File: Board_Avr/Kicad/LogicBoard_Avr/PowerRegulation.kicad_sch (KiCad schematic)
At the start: 8 parts, among them J10 PSU Connector, U3 LM1117-3.3, U4 LM1117-5.0

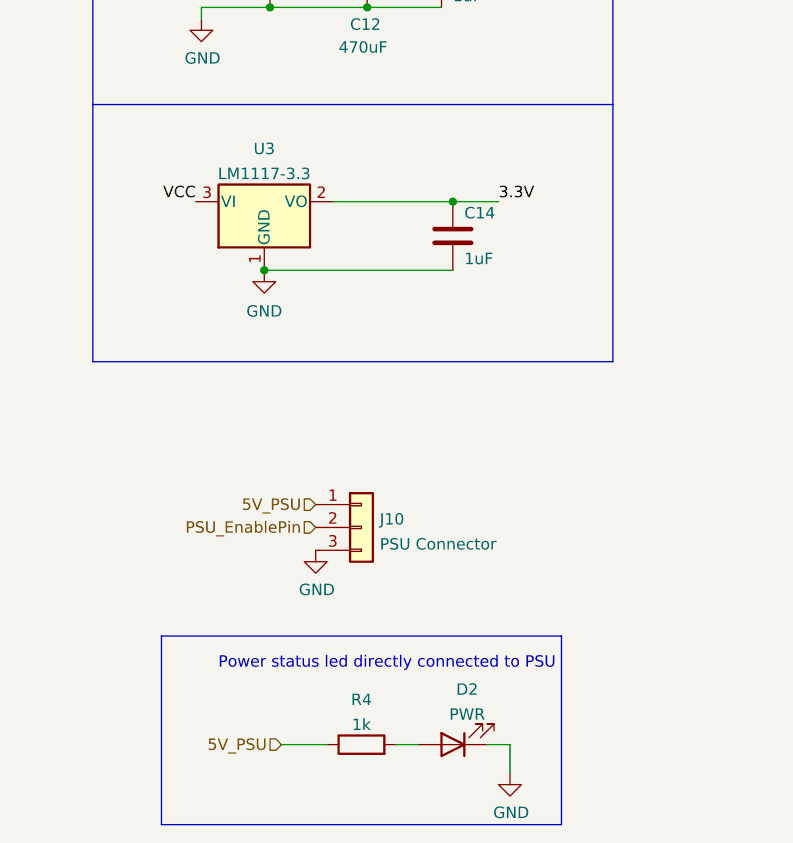
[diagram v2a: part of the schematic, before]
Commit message: Started routing all traces
Signed-off-by: bebenlebricolo <benoittarrade@hotmail.fr>
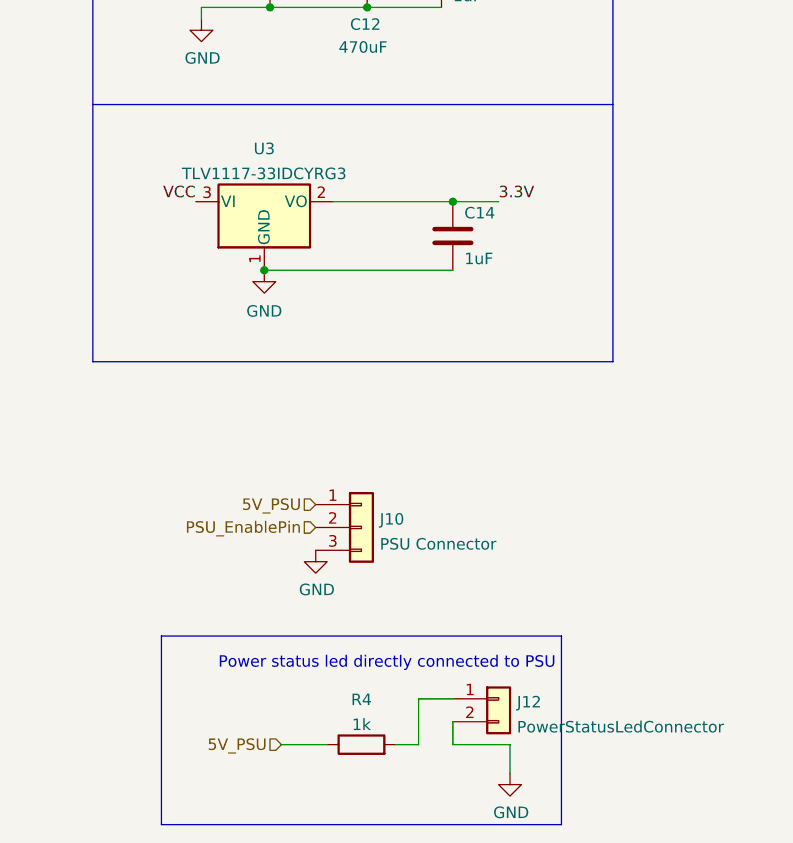
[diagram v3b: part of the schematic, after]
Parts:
- removed D2: PWR, symbol Device:LED
- added J12: PowerStatusLedConnector, Connector_PinHeader_2.54mm:PinHeader_1x02_P2.54mm_Vertical, symbol Connector_Generic:Conn_01x02
- C12: footprint (none) -> Capacitor_SMD:C_Elec_8x6.2
- C13, C14: footprint Capacitor_SMD:C_1206_3216Metric_Pad1.33x1.80mm_HandSolder -> Capacitor_SMD:C_1206_3216Metric
- J10: footprint (none) -> BTS-LogicBoard:559350310
- R4: footprint (none) -> Resistor_SMD:R_1206_3216Metric_Pad1.30x1.75mm_HandSolder
- U3: value LM1117-3.3 -> TLV1117-33IDCYRG3; footprint (none) -> Package_TO_SOT_SMD:SOT-223-3_TabPin2
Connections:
- net GND: now also J12.2 (Pin_2)
- net at R4.2: now also J12.1 (Pin_1)
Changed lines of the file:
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@@
+    (stroke (width 0) (type default) (color 0 0 0 0))
+  )
+  (wire (pts (xy 164.465 118.11) (xy 168.275 118.11))
     (stroke (width 0) (type default) (color 0 0 0 0))
   )
@@
     (stroke (width 0) (type default) (color 0 0 0 0))
   )
+  (wire (pts (xy 164.465 123.19) (xy 164.465 118.11))
+    (stroke (width 0) (type default) (color 0 0 0 0))
+  )
   (polyline (pts (xy 180.34 132.08) (xy 135.89 132.08))
     (stroke (width 0) (type default) (color 0 0 0 0))
@@
     (stroke (width 0) (type default) (color 0 0 0 0))
   )
+  (wire (pts (xy 168.275 120.65) (xy 168.275 123.19))
+    (stroke (width 0) (type default) (color 0 0 0 0))
+  )
   (wire (pts (xy 147.32 70.485) (xy 168.275 70.485))
     (stroke (width 0) (type default) (color 0 0 0 0))
@@
     (stroke (width 0) (type default) (color 0 0 0 0))
   )
-  (wire (pts (xy 172.085 123.19) (xy 174.625 123.19))
+  (wire (pts (xy 168.275 123.19) (xy 174.625 123.19))
     (stroke (width 0) (type default) (color 0 0 0 0))
   )
@@
     (in_bom yes) (on_board yes) (fields_autoplaced)
     (property "Reference" "U3" (id 0) (at 147.32 56.9935 0))
-    (property "Value" "LM1117-3.3" (id 1) (at 147.32 59.7686 0))
-    (property "Footprint" "" (id 2) (at 147.32 62.865 0)
+    (property "Value" "TLV1117-33IDCYRG3" (id 1) (at 147.32 59.7686 0))
+    (property "Footprint" "Package_TO_SOT_SMD:SOT-223-3_TabPin2" (id 2) (at 147.32 62.865 0)
       (effects (font (size 1.27 1.27)) hide)
     )
@@
       (effects (font (size 1.27 1.27)) (justify left))
     )
-    (property "Footprint" "Capacitor_SMD:C_1206_3216Metric_Pad1.33x1.80mm_HandSolder" (id 2) (at 167.9702 41.275 0)
+    (property "Footprint" "Capacitor_SMD:C_1206_3216Metric" (id 2) (at 167.9702 41.275 0)
       (effects (font (size 1.27 1.27)) hide)
     )
@@
       (effects (font (size 1.27 1.27)) (justify left))
     )
-    (property "Footprint" "Capacitor_SMD:C_1206_3216Metric_Pad1.33x1.80mm_HandSolder" (id 2) (at 169.2402 70.485 0)
+    (property "Footprint" "Capacitor_SMD:C_1206_3216Metric" (id 2) (at 169.2402 70.485 0)
       (effects (font (size 1.27 1.27)) hide)
     )
@@
       (effects (font (size 1.27 1.27)) (justify left))
     )
-    (property "Footprint" "" (id 2) (at 158.115 99.06 0)
+    (property "Footprint" "BTS-LogicBoard:559350310" (id 2) (at 158.115 99.06 0)
       (effects (font (size 1.27 1.27)) hide)
     )
@@
     (property "Reference" "R4" (id 0) (at 158.115 118.2075 90))
     (property "Value" "1k" (id 1) (at 158.115 120.9826 90))
-    (property "Footprint" "" (id 2) (at 158.115 124.968 90)
+    (property "Footprint" "Resistor_SMD:R_1206_3216Metric_Pad1.30x1.75mm_HandSolder" (id 2) (at 158.115 124.968 90)
       (effects (font (size 1.27 1.27)) hide)
     )
@@
     (pin "2")
   )
-  (symbol (lib_id "Device:LED") (at 168.275 123.19 180) (unit 1)
-    (in_bom yes) (on_board yes) (fields_autoplaced)
-    (property "Reference" "D2" (id 0) (at 169.8625 117.0645 0))
-    (property "Value" "PWR" (id 1) (at 169.8625 119.8396 0))
-    (property "Footprint" "" (id 2) (at 168.275 123.19 0)
-      (effects (font (size 1.27 1.27)) hide)
-    )
-    (property "Datasheet" "~" (id 3) (at 168.275 123.19 0)
+  (symbol (lib_id "Connector_Generic:Conn_01x02") (at 173.355 118.11 0) (unit 1)
+    (in_bom yes) (on_board yes) (fields_autoplaced)
+    (property "Reference" "J12" (id 0) (at 175.387 118.4715 0)
+      (effects (font (size 1.27 1.27)) (justify left))
+    )
+    (property "Value" "PowerStatusLedConnector" (id 1) (at 175.387 121.2466 0)
+      (effects (font (size 1.27 1.27)) (justify left))
+    )
+    (property "Footprint" "Connector_PinHeader_2.54mm:PinHeader_1x02_P2.54mm_Vertical" (id 2) (at 173.355 118.11 0)
+      (effects (font (size 1.27 1.27)) hide)
+    )
+    (property "Datasheet" "~" (id 3) (at 173.355 118.11 0)
       (effects (font (size 1.27 1.27)) hide)
     )
@@
       (effects (font (size 1.27 1.27)) (justify left))
     )
-    (property "Footprint" "" (id 2) (at 159.7152 41.275 0)
-      (effects (font (size 1.27 1.27)) hide)
-    )
+    (property "Footprint" "Capacitor_SMD:C_Elec_8x6.2" (id 2) (at 159.7152 41.275 0)
+      (effects (font (size 1.27 1.27)) hide)
+    )

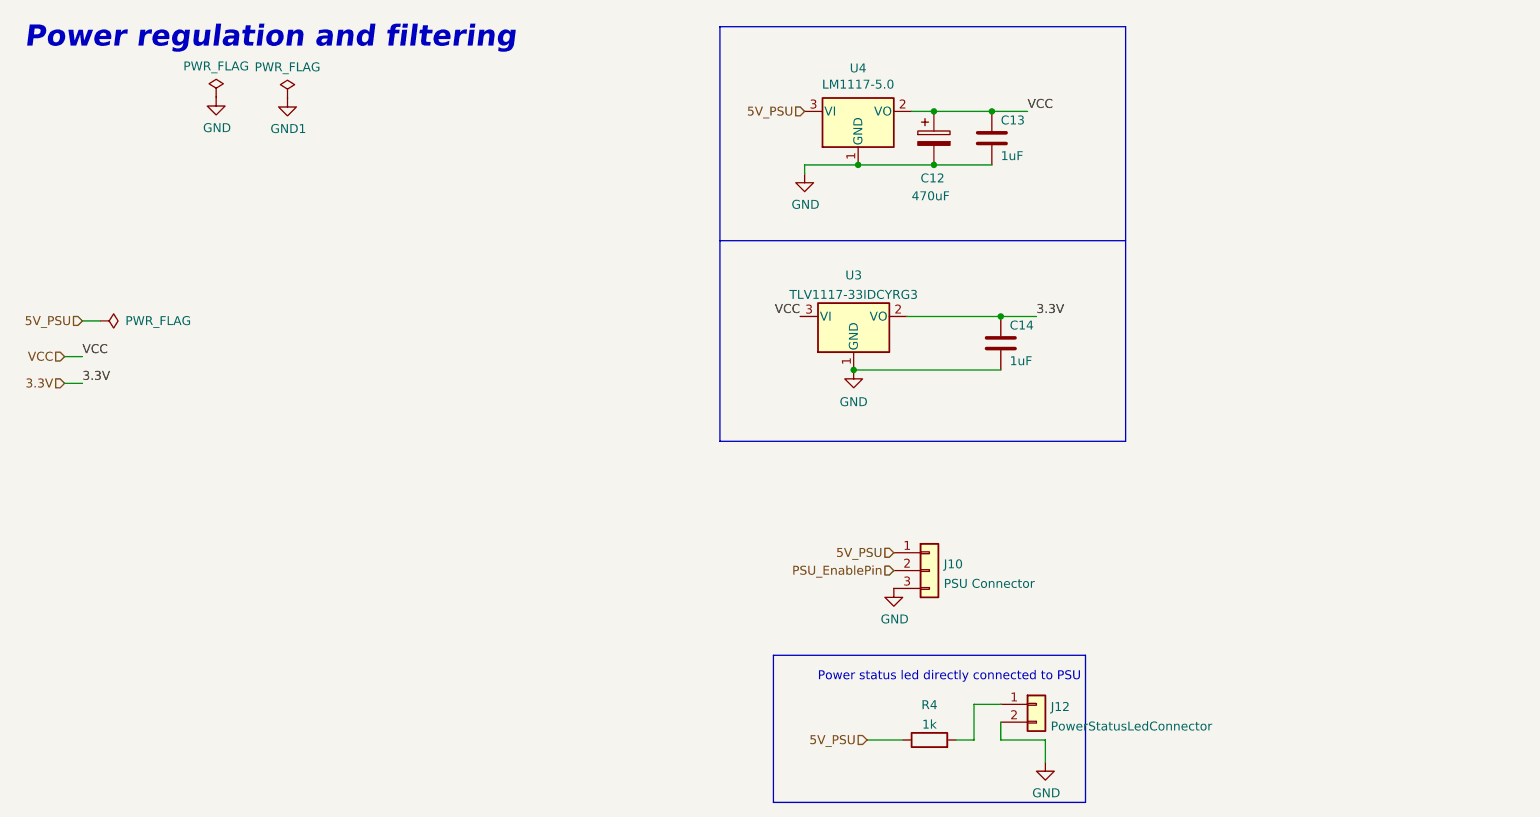
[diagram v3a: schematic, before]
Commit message: Tweaked top silkscreen to embed useful information
Signed-off-by: bebenlebricolo <benoittarrade@hotmail.fr>
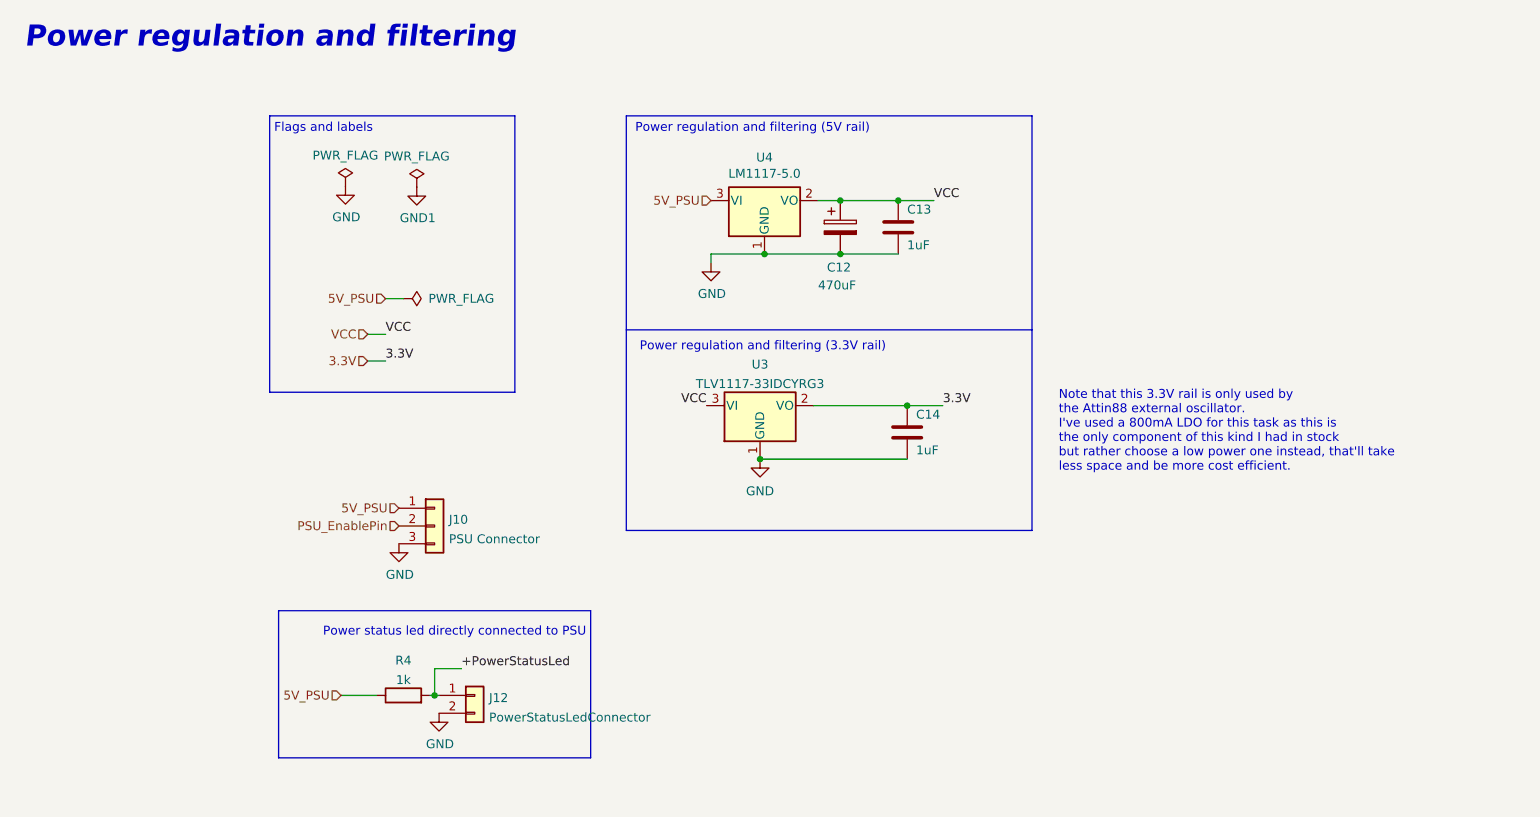
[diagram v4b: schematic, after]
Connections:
- net +PowerStatusLed: now reaches J12.1 (Pin_1), R4.2
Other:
- note added: "Flags and labels"
- note added: "Note that this 3.3V rail is only used by the Attin88 external oscillator. I've used a 800mA LDO for this task as this is the only component of this kind I had in stock but rather choose a low power one instead, that'll take less space and be more cost efficient."
- note added: "Power regulation and filtering (3.3V rail)"
- note added: "Power regulation and filtering (5V rail)"
- moved on the sheet: C12, C13, C14, J10, J12, R4, U3, U4

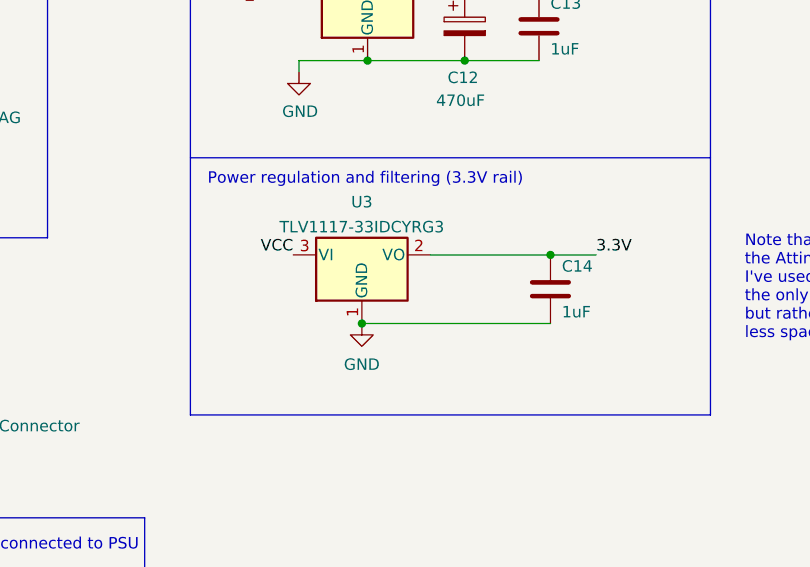
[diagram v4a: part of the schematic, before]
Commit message: Replaced TLV1117-3.3 by NCP630SN330 and polished a bit zoning
Signed-off-by: bebenlebricolo <benoittarrade@hotmail.fr>
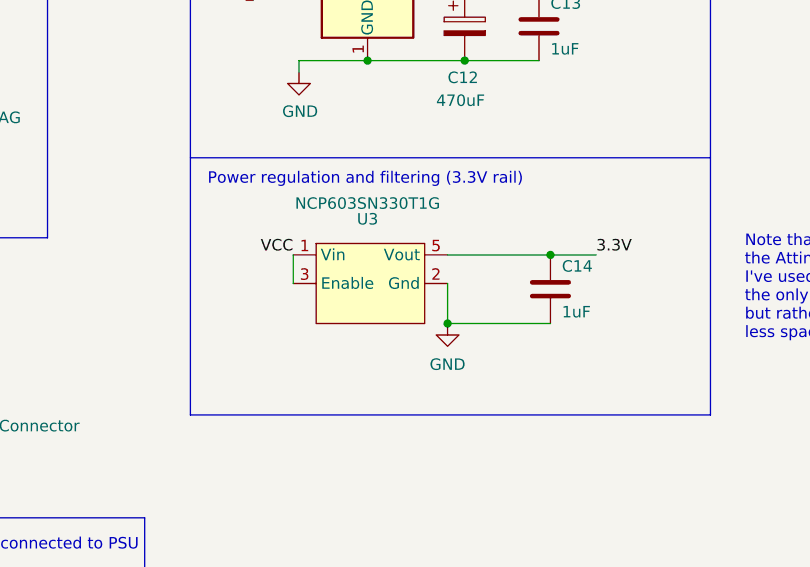
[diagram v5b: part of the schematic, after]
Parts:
- U3: value TLV1117-33IDCYRG3 -> NCP603SN330T1G; footprint Package_TO_SOT_SMD:SOT-223-3_TabPin2 -> Package_SO:TSOP-5_1.65x3.05mm_P0.95mm; symbol Regulator_Linear:LM1117-3.3 -> BTS-LogicBoard:NCP603SN330T1G
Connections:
- net 3.3V: now also U3.5 (Vout); no longer U3.2 (VO)
- net GND: now also U3.2 (Gnd); no longer U3.1 (GND)
- net VCC: now also U3.1 (Vin)
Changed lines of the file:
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@@
   (junction (at 145.415 53.975) (diameter 0) (color 0 0 0 0)
   )
-  (junction (at 133.985 83.185) (diameter 0) (color 0 0 0 0)
-  )
   (junction (at 145.415 46.355) (diameter 0) (color 0 0 0 0)
   )
@@
   (junction (at 134.62 53.975) (diameter 0) (color 0 0 0 0)
   )
+  (junction (at 143.51 83.185) (diameter 0) (color 0 0 0 0)
+  )
   (junction (at 87.63 116.84) (diameter 0) (color 0 0 0 0)
   )
@@
     (stroke (width 0) (type default) (color 0 0 0 0))
   )
+  (wire (pts (xy 143.51 78.74) (xy 143.51 83.185))
+    (stroke (width 0) (type default) (color 0 0 0 0))
+  )
   (polyline (pts (xy 64.135 34.29) (xy 64.135 73.66))
     (stroke (width 0) (type default) (color 0 0 0 0))
@@
     (stroke (width 0) (type default) (color 0 0 0 0))
   )
+  (wire (pts (xy 143.51 83.185) (xy 154.94 83.185))
+    (stroke (width 0) (type default) (color 0 0 0 0))
+  )
   (wire (pts (xy 78.105 65.405) (xy 80.645 65.405))
     (stroke (width 0) (type default) (color 0 0 0 0))
@@
     (stroke (width 0) (type default) (color 0 0 0 0))
   )
+  (wire (pts (xy 143.51 75.565) (xy 154.94 75.565))
+    (stroke (width 0) (type default) (color 0 0 0 0))
+  )
   (wire (pts (xy 127 53.975) (xy 134.62 53.975))
     (stroke (width 0) (type default) (color 0 0 0 0))
   )
-  (wire (pts (xy 141.605 75.565) (xy 154.94 75.565))
-    (stroke (width 0) (type default) (color 0 0 0 0))
-  )
   (polyline (pts (xy 114.935 34.29) (xy 114.935 93.345))
     (stroke (width 0) (type default) (color 0 0 0 0))
@@
     (stroke (width 0) (type default) (color 0 0 0 0))
   )
-  (wire (pts (xy 133.985 83.185) (xy 154.94 83.185))
+  (wire (pts (xy 126.365 75.565) (xy 126.365 78.74))
     (stroke (width 0) (type default) (color 0 0 0 0))
   )
@@
     (pin "1")
   )
-  (symbol (lib_id "Regulator_Linear:LM1117-3.3") (at 133.985 75.565 0) (unit 1)
-    (in_bom yes) (on_board yes) (fields_autoplaced)
-    (property "Reference" "U3" (id 0) (at 133.985 69.6935 0))
-    (property "Value" "TLV1117-33IDCYRG3" (id 1) (at 133.985 72.4686 0))
-    (property "Footprint" "Package_TO_SOT_SMD:SOT-223-3_TabPin2" (id 2) (at 133.985 75.565 0)
-      (effects (font (size 1.27 1.27)) hide)
-    )
-    (property "Datasheet" "http://www.ti.com/lit/ds/symlink/lm1117.pdf" (id 3) (at 133.985 75.565 0)
+  (symbol (lib_id "BTS-LogicBoard:NCP603SN330T1G") (at 134.62 77.47 0) (unit 1)
+    (in_bom yes) (on_board yes)
+    (property "Reference" "U3" (id 0) (at 134.62 71.5985 0))
+    (property "Value" "NCP603SN330T1G" (id 1) (at 134.62 69.85 0))
+    (property "Footprint" "Package_SO:TSOP-5_1.65x3.05mm_P0.95mm" (id 2) (at 137.795 87.63 0)
+      (effects (font (size 1.27 1.27)) hide)
+    )
+    (property "Datasheet" "https://www.onsemi.com/pdf/datasheet/ncp603-d.pdf" (id 3) (at 138.43 89.535 0)
       (effects (font (size 1.27 1.27)) hide)
     )
@@
     (pin "2")
     (pin "3")
+    (pin "4")
+    (pin "5")
   )
   (symbol (lib_id "Device:C") (at 153.67 50.165 0) (unit 1)
@@
     (pin "3")
   )
-  (symbol (lib_id "power:GND") (at 133.985 83.185 0) (unit 1)
+  (symbol (lib_id "power:GND") (at 143.51 83.185 0) (unit 1)
     (in_bom yes) (on_board yes) (fields_autoplaced)
-    (property "Reference" "#PWR0129" (id 0) (at 133.985 89.535 0)
-      (effects (font (size 1.27 1.27)) hide)
-    )
-    (property "Value" "GND" (id 1) (at 133.985 87.7475 0))
-    (property "Footprint" "" (id 2) (at 133.985 83.185 0)
-      (effects (font (size 1.27 1.27)) hide)
-    )
-    (property "Datasheet" "" (id 3) (at 133.985 83.185 0)
-      (effects (font (size 1.27 1.27)) hide)
-    )
+    (property "Reference" "#PWR0129" (id 0) (at 143.51 89.535 0)
+      (effects (font (size 1.27 1.27)) hide)
+    )
+    (property "Value" "GND" (id 1) (at 143.51 87.7475 0))
+    (property "Footprint" "" (id 2) (at 143.51 83.185 0)
+      (effects (font (size 1.27 1.27)) hide)
+    )
+    (property "Datasheet" "" (id 3) (at 143.51 83.185 0)
+      (effects (font (size 1.27 1.27)) hide)
+    )
